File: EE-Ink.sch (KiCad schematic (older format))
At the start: 14 parts

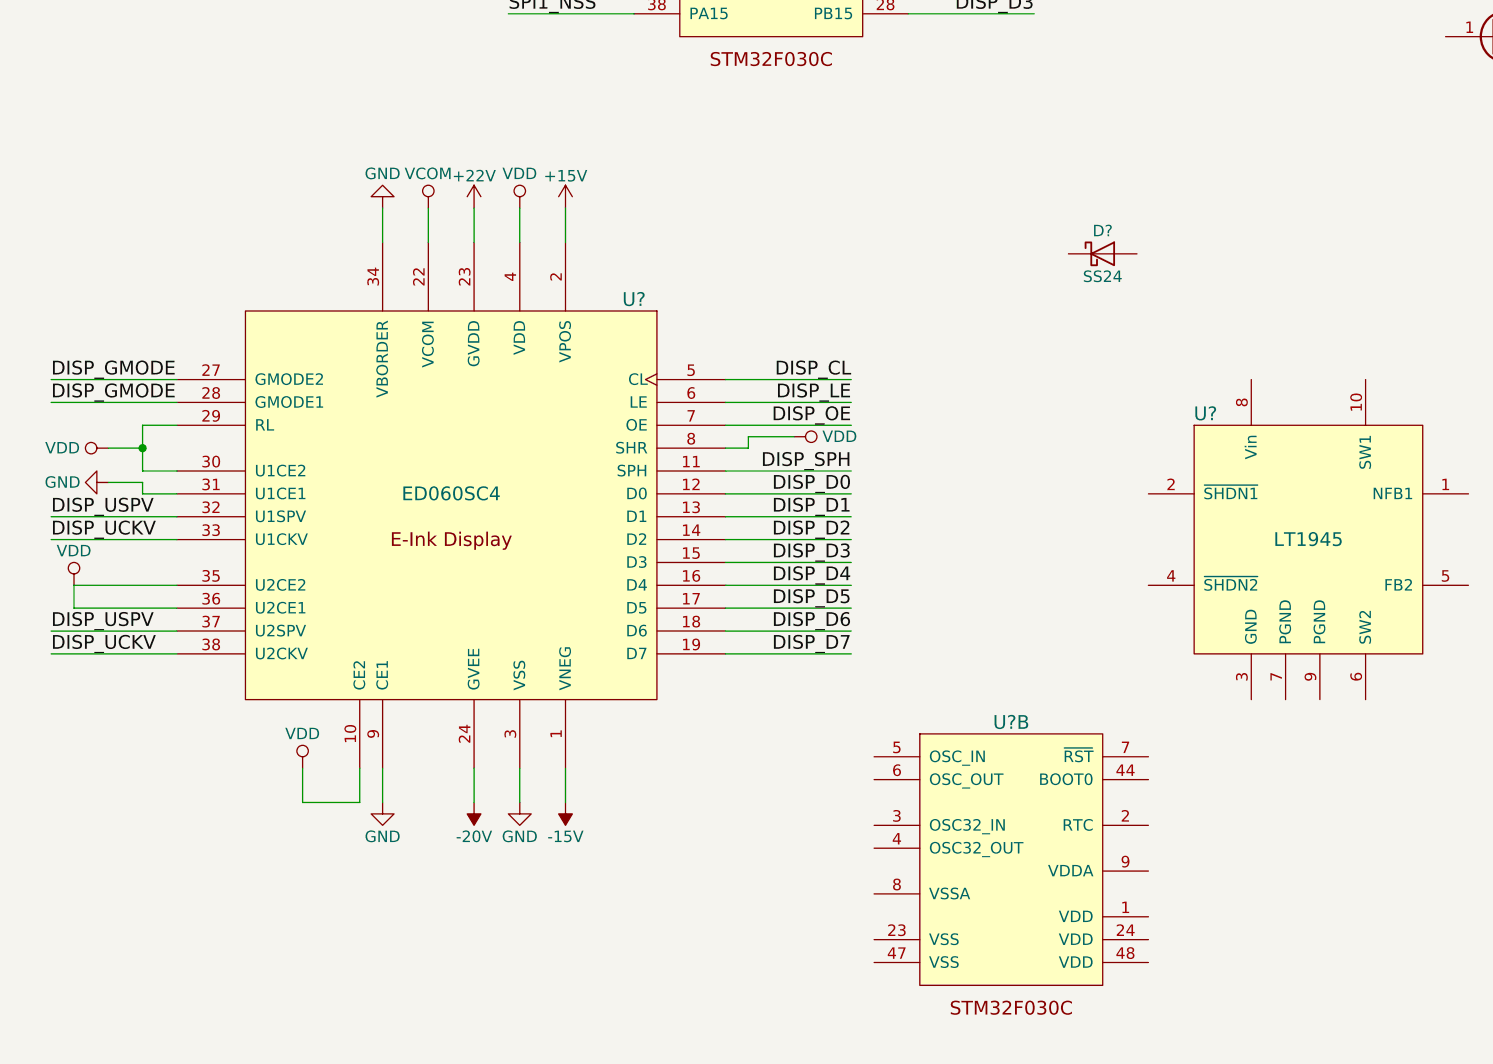
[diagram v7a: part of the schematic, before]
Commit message: Minor changes to connections to display.
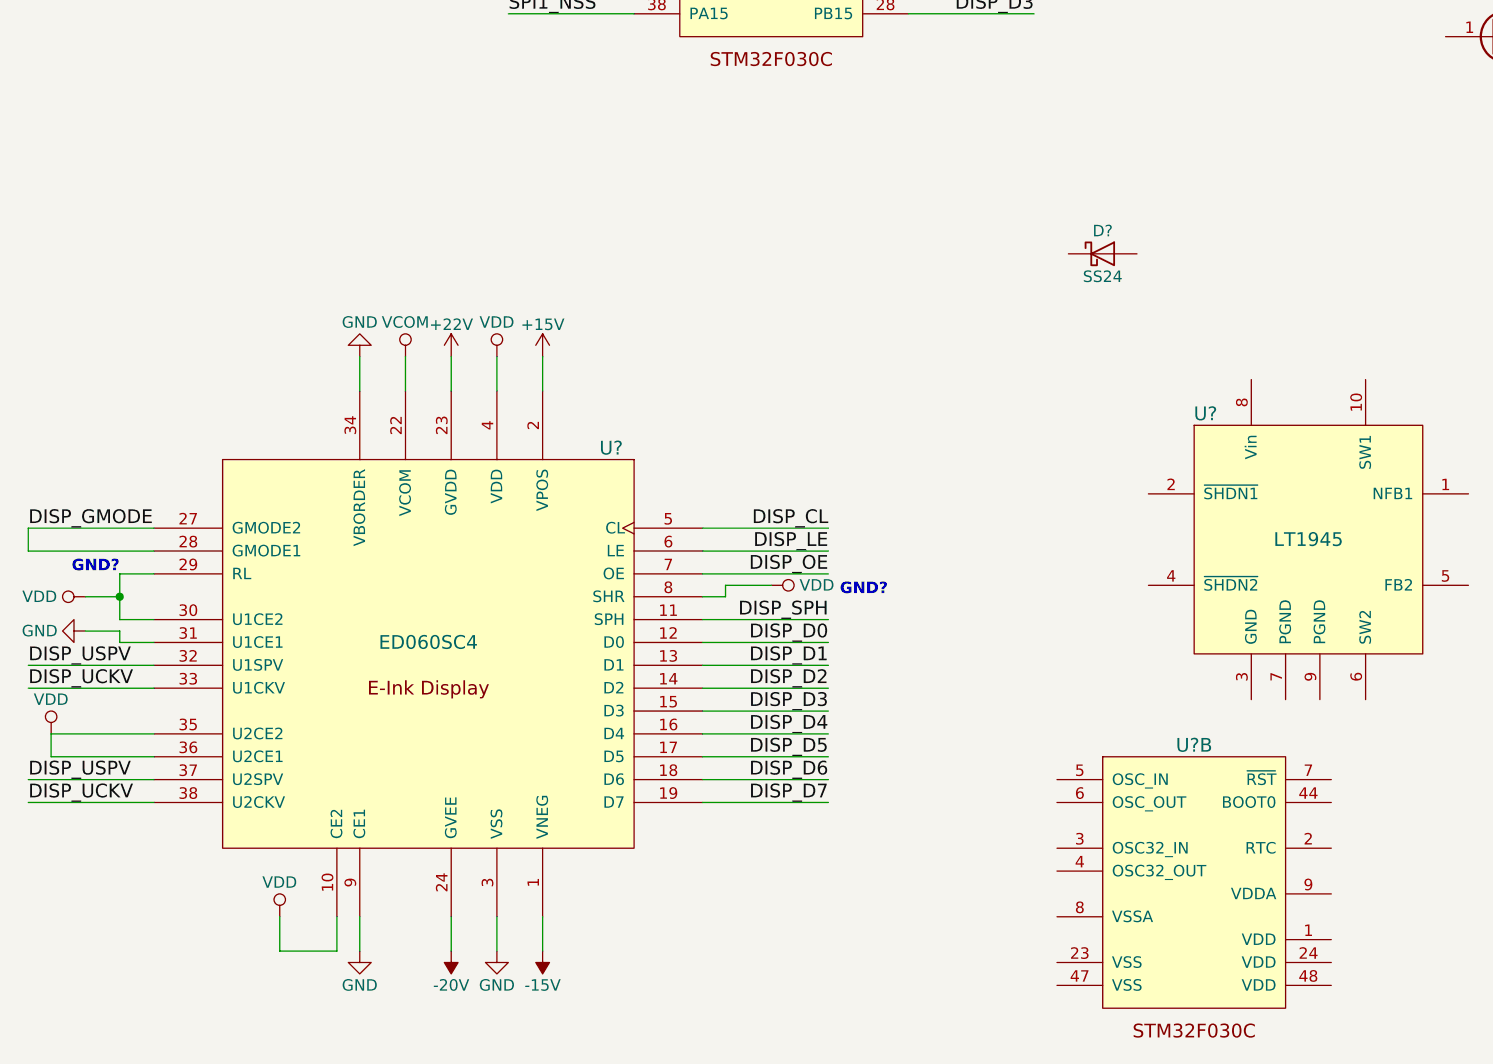
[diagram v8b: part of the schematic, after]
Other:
- note added: "GND?"
- moved on the sheet: U?, U?B
